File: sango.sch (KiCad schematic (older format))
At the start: 22 parts

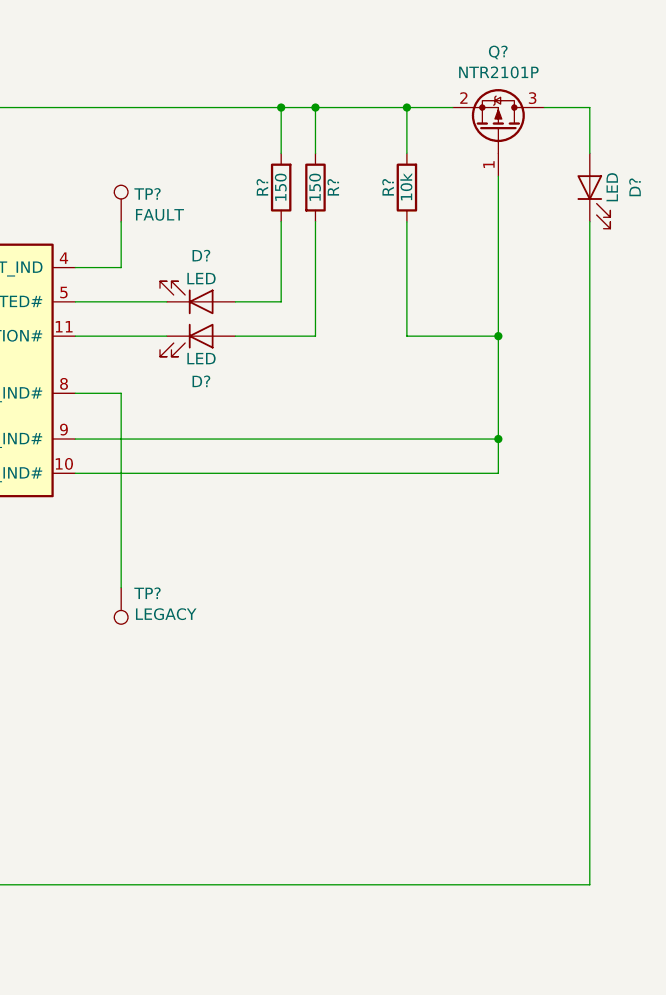
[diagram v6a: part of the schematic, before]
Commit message: add ilim R for output LED
- part numbers for remaining resistors
- rename LEDs for associated color
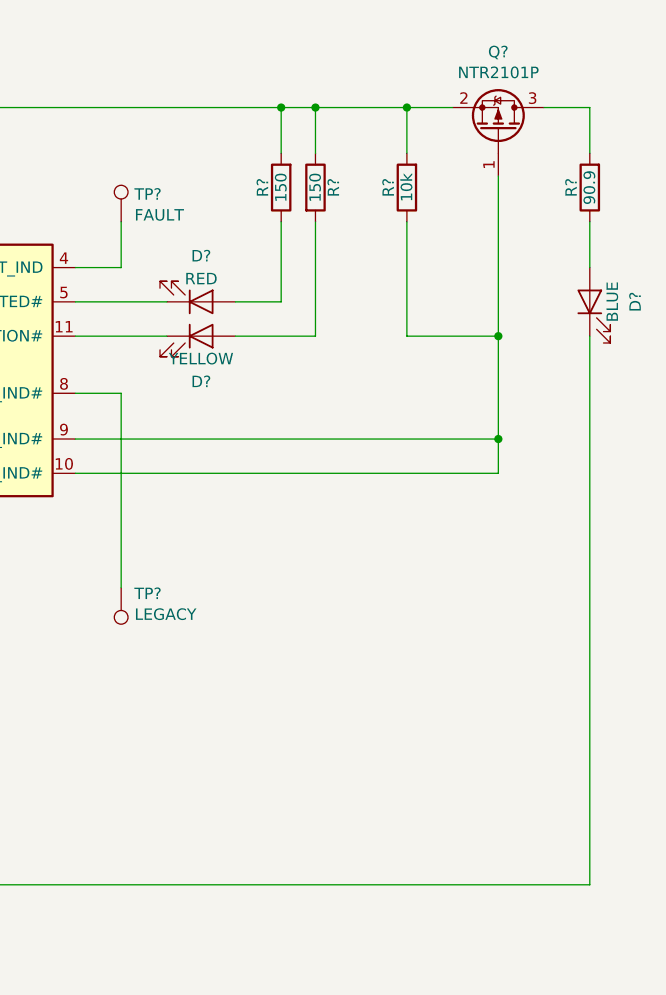
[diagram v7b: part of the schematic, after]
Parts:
- added R?: 90.9, symbol Device:R
- D?: value LED -> YELLOW
- D?: value LED -> RED
- D?: value LED -> BLUE
- R? (x2): Description (none) -> RES SMD 150 OHM 1% 1/10W 0603; Manufacturer (none) -> Panasonic Electronic Components; Manufacturer Part Number (none) -> ERJ-3EKF1500V; Supplier (none) -> Digi-Key; Supplier Part Number (none) -> P150HCT-ND
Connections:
- net at Q?.3 (D): now also R?.2; no longer D?.2 (A)
- new net: D?.2 (A), R?.1
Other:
- moved on the sheet: D?
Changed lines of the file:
@@
 P 7650 3000
 F 0 "D?" H 7650 2800 50  0000 C CNN
-F 1 "LED" H 7650 2900 50  0000 C CNN
+F 1 "YELLOW" H 7650 2900 50  0000 C CNN
 F 2 "" H 7650 3000 50  0001 C CNN
 F 3 "~" H 7650 3000 50  0001 C CNN
@@
 P 7650 2850
 F 0 "D?" H 7650 2650 50  0000 C CNN
-F 1 "LED" H 7650 2750 50  0000 C CNN
+F 1 "RED" H 7650 2750 50  0000 C CNN
 F 2 "" H 7650 2850 50  0001 C CNN
 F 3 "~" H 7650 2850 50  0001 C CNN
@@
 F 1 "150" V 8000 2350 50  0000 C CNN
 F 2 "" V 7930 2350 50  0001 C CNN
-F 3 "" H 8000 2350 50  0001 C CNN
+F 3 "https://industrial.panasonic.com/cdbs/www-data/pdf/RDA0000/AOA0000C304.pdf" H 8000 2350 50  0001 C CNN
+F 4 "RES SMD 150 OHM 1% 1/10W 0603" H 0   0   50  0001 C CNN "Description"
+F 5 "Panasonic Electronic Components" H 0   0   50  0001 C CNN "Manufacturer"
+F 6 "ERJ-3EKF1500V" H 0   0   50  0001 C CNN "Manufacturer Part Number"
+F 7 "Digi-Key" H 0   0   50  0001 C CNN "Supplier"
+F 8 "P150HCT-ND" H 0   0   50  0001 C CNN "Supplier Part Number"
 	1    8000 2350
 	-1   0    0    1
@@
 F 1 "150" V 8150 2350 50  0000 C CNN
 F 2 "" V 8080 2350 50  0001 C CNN
-F 3 "" H 8150 2350 50  0001 C CNN
+F 3 "https://industrial.panasonic.com/cdbs/www-data/pdf/RDA0000/AOA0000C304.pdf" H 8150 2350 50  0001 C CNN
+F 4 "RES SMD 150 OHM 1% 1/10W 0603" H 0   0   50  0001 C CNN "Description"
+F 5 "Panasonic Electronic Components" H 0   0   50  0001 C CNN "Manufacturer"
+F 6 "ERJ-3EKF1500V" H 0   0   50  0001 C CNN "Manufacturer Part Number"
+F 7 "Digi-Key" H 0   0   50  0001 C CNN "Supplier"
+F 8 "P150HCT-ND" H 0   0   50  0001 C CNN "Supplier Part Number"
 	1    8150 2350
 	1    0    0    -1
@@
 L Device:LED D?
 U 1 1 5BF7A803
-P 9350 2350
-F 0 "D?" H 9350 2150 50  0000 C CNN
-F 1 "LED" H 9350 2250 50  0000 C CNN
-F 2 "" H 9350 2350 50  0001 C CNN
-F 3 "~" H 9350 2350 50  0001 C CNN
-	1    9350 2350
+P 9350 2850
+F 0 "D?" H 9350 2650 50  0000 C CNN
+F 1 "BLUE" H 9350 2750 50  0000 C CNN
+F 2 "" H 9350 2850 50  0001 C CNN
+F 3 "~" H 9350 2850 50  0001 C CNN
+	1    9350 2850
 	0    -1   -1   0
 $EndComp
@@
 Wire Wire Line
 	9350 2000 9350 2200
-Wire Wire Line
-	9350 2500 9350 5400
 Wire Wire Line
 	9350 5400 6300 5400
@@
 Wire Wire Line
 	6200 5400 6300 5400
+$Comp
+L Device:R R?
+U 1 1 5BF89938
+P 9350 2350
+F 0 "R?" V 9430 2350 50  0000 C CNN
+F 1 "90.9" V 9350 2350 50  0000 C CNN
+F 2 "" V 9280 2350 50  0001 C CNN
+F 3 "https://industrial.panasonic.com/cdbs/www-data/pdf/RDA0000/AOA0000C304.pdf" H 9350 2350 50  0001 C CNN
+F 4 "RES SMD 90.9 OHM 1% 1/10W 0603" H 0   0   50  0001 C CNN "Description"
+F 5 "Panasonic Electronic Components" H 0   0   50  0001 C CNN "Manufacturer"
+F 6 "ERJ-3EKF90R9V" H 0   0   50  0001 C CNN "Manufacturer Part Number"
+F 7 "Digi-Key" H 0   0   50  0001 C CNN "Supplier"
+F 8 "P90.9HCT-ND" H 0   0   50  0001 C CNN "Supplier Part Number"
+	1    9350 2350
+	-1   0    0    1
+$EndComp
+Wire Wire Line
+	9350 2500 9350 2700
+Wire Wire Line
+	9350 3000 9350 5400
 $EndSCHEMATC

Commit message: switch resistors from 0603 --> 0805
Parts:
- R? (x5): Description RES SMD 10K OHM 1% 1/10W 0603 -> RES SMD 10K OHM 1% 1/8W 0805; Manufacturer Part Number ERJ-3EKF1002V -> ERJ-6ENF1002V; Supplier Part Number P10.0KHCT-ND -> P10.0KCCT-ND
- R? (x3): Description RES SMD 5.1K OHM 1% 1/10W 0603 -> RES SMD 5.1K OHM 1% 1/8W 0805; Manufacturer Part Number ERJ-3EKF5101V -> ERJ-6ENF5101V; Supplier Part Number P5.10KHCT-ND -> P5.10KCCT-ND
- R?: Description RES SMD 35.7K OHM 1% 1/10W 0603 -> RES SMD 35.7K OHM 1% 1/8W 0805; Manufacturer Part Number ERJ-3EKF3572V -> ERJ-6ENF3572V; Supplier Part Number P35.7KHCT-ND -> P35.7KCCT-ND
- R?: Description RES SMD 1M OHM 1% 1/10W 0603 -> RES SMD 1M OHM 1% 1/8W 0805; Manufacturer Part Number ERJ-3EKF1004V -> ERJ-6ENF1004V; Supplier Part Number P1.00MHCT-ND -> P1.00MCCT-ND
- R? (x2): Description RES SMD 150 OHM 1% 1/10W 0603 -> RES SMD 150 OHM 1% 1/8W 0805; Manufacturer Part Number ERJ-3EKF1500V -> ERJ-6ENF1500V; Supplier Part Number P150HCT-ND -> P150CCT-ND
- R?: Description RES SMD 90.9 OHM 1% 1/10W 0603 -> RES SMD 90.9 OHM 1% 1/8W 0805; Manufacturer Part Number ERJ-3EKF90R9V -> ERJ-6ENF90R9V; Supplier Part Number P90.9HCT-ND -> P90.9CCT-ND
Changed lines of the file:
@@
 F 2 "" V 4680 3450 50  0001 C CNN
 F 3 "https://industrial.panasonic.com/cdbs/www-data/pdf/RDA0000/AOA0000C304.pdf" H 4750 3450 50  0001 C CNN
-F 4 "RES SMD 10K OHM 1% 1/10W 0603" H 4750 3450 50  0001 C CNN "Description"
+F 4 "RES SMD 10K OHM 1% 1/8W 0805" H 4750 3450 50  0001 C CNN "Description"
 F 5 "Panasonic Electronic Components" H 4750 3450 50  0001 C CNN "Manufacturer"
-F 6 "ERJ-3EKF1002V" H 4750 3450 50  0001 C CNN "Manufacturer Part Number"
+F 6 "ERJ-6ENF1002V" H 4750 3450 50  0001 C CNN "Manufacturer Part Number"
 F 7 "Digi-Key" H 4750 3450 50  0001 C CNN "Supplier"
-F 8 "P10.0KHCT-ND" H 4750 3450 50  0001 C CNN "Supplier Part Number"
+F 8 "P10.0KCCT-ND" H 4750 3450 50  0001 C CNN "Supplier Part Number"
 	1    4750 3450
 	0    -1   -1   0
@@
 F 2 "" V 4680 3600 50  0001 C CNN
 F 3 "https://industrial.panasonic.com/cdbs/www-data/pdf/RDA0000/AOA0000C304.pdf" H 4750 3600 50  0001 C CNN
-F 4 "RES SMD 10K OHM 1% 1/10W 0603" H 4750 3600 50  0001 C CNN "Description"
+F 4 "RES SMD 10K OHM 1% 1/8W 0805" H 4750 3600 50  0001 C CNN "Description"
 F 5 "Panasonic Electronic Components" H 4750 3600 50  0001 C CNN "Manufacturer"
-F 6 "ERJ-3EKF1002V" H 4750 3600 50  0001 C CNN "Manufacturer Part Number"
+F 6 "ERJ-6ENF1002V" H 4750 3600 50  0001 C CNN "Manufacturer Part Number"
 F 7 "Digi-Key" H 4750 3600 50  0001 C CNN "Supplier"
-F 8 "P10.0KHCT-ND" H 4750 3600 50  0001 C CNN "Supplier Part Number"
+F 8 "P10.0KCCT-ND" H 4750 3600 50  0001 C CNN "Supplier Part Number"
 	1    4750 3600
 	0    1    1    0
@@
 F 2 "" V 4330 3950 50  0001 C CNN
 F 3 "https://industrial.panasonic.com/cdbs/www-data/pdf/RDA0000/AOA0000C304.pdf" H 4400 3950 50  0001 C CNN
-F 4 "RES SMD 5.1K OHM 1% 1/10W 0603" H 4400 3950 50  0001 C CNN "Description"
+F 4 "RES SMD 5.1K OHM 1% 1/8W 0805" H 4400 3950 50  0001 C CNN "Description"
 F 5 "Panasonic Electronic Components" H 4400 3950 50  0001 C CNN "Manufacturer"
-F 6 "ERJ-3EKF5101V" H 4400 3950 50  0001 C CNN "Manufacturer Part Number"
+F 6 "ERJ-6ENF5101V" H 4400 3950 50  0001 C CNN "Manufacturer Part Number"
 F 7 "Digi-Key" H 4400 3950 50  0001 C CNN "Supplier"
-F 8 "P5.10KHCT-ND" H 4400 3950 50  0001 C CNN "Supplier Part Number"
+F 8 "P5.10KCCT-ND" H 4400 3950 50  0001 C CNN "Supplier Part Number"
 	1    4400 3950
 	1    0    0    -1
@@
 F 2 "" V 4180 3950 50  0001 C CNN
 F 3 "https://industrial.panasonic.com/cdbs/www-data/pdf/RDA0000/AOA0000C304.pdf" H 4250 3950 50  0001 C CNN
-F 4 "RES SMD 5.1K OHM 1% 1/10W 0603" H 4250 3950 50  0001 C CNN "Description"
+F 4 "RES SMD 5.1K OHM 1% 1/8W 0805" H 4250 3950 50  0001 C CNN "Description"
 F 5 "Panasonic Electronic Components" H 4250 3950 50  0001 C CNN "Manufacturer"
-F 6 "ERJ-3EKF5101V" H 4250 3950 50  0001 C CNN "Manufacturer Part Number"
+F 6 "ERJ-6ENF5101V" H 4250 3950 50  0001 C CNN "Manufacturer Part Number"
 F 7 "Digi-Key" H 4250 3950 50  0001 C CNN "Supplier"
-F 8 "P5.10KHCT-ND" H 4250 3950 50  0001 C CNN "Supplier Part Number"
+F 8 "P5.10KCCT-ND" H 4250 3950 50  0001 C CNN "Supplier Part Number"
 	1    4250 3950
 	-1   0    0    1
@@
 F 2 "" V 4930 2350 50  0001 C CNN
 F 3 "https://industrial.panasonic.com/cdbs/www-data/pdf/RDA0000/AOA0000C304.pdf" H 5000 2350 50  0001 C CNN
-F 4 "RES SMD 10K OHM 1% 1/10W 0603" H 5000 2350 50  0001 C CNN "Description"
+F 4 "RES SMD 10K OHM 1% 1/8W 0805" H 5000 2350 50  0001 C CNN "Description"
 F 5 "Panasonic Electronic Components" H 5000 2350 50  0001 C CNN "Manufacturer"
-F 6 "ERJ-3EKF1002V" H 5000 2350 50  0001 C CNN "Manufacturer Part Number"
+F 6 "ERJ-6ENF1002V" H 5000 2350 50  0001 C CNN "Manufacturer Part Number"
 F 7 "Digi-Key" H 5000 2350 50  0001 C CNN "Supplier"
-F 8 "P10.0KHCT-ND" H 5000 2350 50  0001 C CNN "Supplier Part Number"
+F 8 "P10.0KCCT-ND" H 5000 2350 50  0001 C CNN "Supplier Part Number"
 	1    5000 2350
 	-1   0    0    1
@@
 F 2 "" V 5080 2350 50  0001 C CNN
 F 3 "https://industrial.panasonic.com/cdbs/www-data/pdf/RDA0000/AOA0000C304.pdf" H 5150 2350 50  0001 C CNN
-F 4 "RES SMD 10K OHM 1% 1/10W 0603" H 5150 2350 50  0001 C CNN "Description"
+F 4 "RES SMD 10K OHM 1% 1/8W 0805" H 5150 2350 50  0001 C CNN "Description"
 F 5 "Panasonic Electronic Components" H 5150 2350 50  0001 C CNN "Manufacturer"
-F 6 "ERJ-3EKF1002V" H 5150 2350 50  0001 C CNN "Manufacturer Part Number"
+F 6 "ERJ-6ENF1002V" H 5150 2350 50  0001 C CNN "Manufacturer Part Number"
 F 7 "Digi-Key" H 5150 2350 50  0001 C CNN "Supplier"
-F 8 "P10.0KHCT-ND" H 5150 2350 50  0001 C CNN "Supplier Part Number"
+F 8 "P10.0KCCT-ND" H 5150 2350 50  0001 C CNN "Supplier Part Number"
 	1    5150 2350
 	1    0    0    -1
@@
 F 2 "" V 3880 3250 50  0001 C CNN
 F 3 "https://industrial.panasonic.com/cdbs/www-data/pdf/RDA0000/AOA0000C304.pdf" H 3950 3250 50  0001 C CNN
-F 4 "RES SMD 5.1K OHM 1% 1/10W 0603" H 3950 3250 50  0001 C CNN "Description"
+F 4 "RES SMD 5.1K OHM 1% 1/8W 0805" H 3950 3250 50  0001 C CNN "Description"
 F 5 "Panasonic Electronic Components" H 3950 3250 50  0001 C CNN "Manufacturer"
-F 6 "ERJ-3EKF5101V" H 3950 3250 50  0001 C CNN "Manufacturer Part Number"
+F 6 "ERJ-6ENF5101V" H 3950 3250 50  0001 C CNN "Manufacturer Part Number"
 F 7 "Digi-Key" H 3950 3250 50  0001 C CNN "Supplier"
-F 8 "P5.10KHCT-ND" H 3950 3250 50  0001 C CNN "Supplier Part Number"
+F 8 "P5.10KCCT-ND" H 3950 3250 50  0001 C CNN "Supplier Part Number"
 	1    3950 3250
 	-1   0    0    1
@@
 F 2 "" V 3880 2850 50  0001 C CNN
 F 3 "https://industrial.panasonic.com/cdbs/www-data/pdf/RDA0000/AOA0000C304.pdf" H 3950 2850 50  0001 C CNN
-F 4 "RES SMD 35.7K OHM 1% 1/10W 0603" H 3950 2850 50  0001 C CNN "Description"
+F 4 "RES SMD 35.7K OHM 1% 1/8W 0805" H 3950 2850 50  0001 C CNN "Description"
 F 5 "Panasonic Electronic Components" H 3950 2850 50  0001 C CNN "Manufacturer"
-F 6 "ERJ-3EKF3572V" H 3950 2850 50  0001 C CNN "Manufacturer Part Number"
+F 6 "ERJ-6ENF3572V" H 3950 2850 50  0001 C CNN "Manufacturer Part Number"
 F 7 "Digi-Key" H 3950 2850 50  0001 C CNN "Supplier"
-F 8 "P35.7KHCT-ND" H 3950 2850 50  0001 C CNN "Supplier Part Number"
+F 8 "P35.7KCCT-ND" H 3950 2850 50  0001 C CNN "Supplier Part Number"
 	1    3950 2850
 	-1   0    0    1
@@
 F 2 "" V 2580 5150 50  0001 C CNN
 F 3 "https://industrial.panasonic.com/cdbs/www-data/pdf/RDA0000/AOA0000C304.pdf" H 2650 5150 50  0001 C CNN
-F 4 "RES SMD 1M OHM 1% 1/10W 0603" H 2650 5150 50  0001 C CNN "Description"
+F 4 "RES SMD 1M OHM 1% 1/8W 0805" H 2650 5150 50  0001 C CNN "Description"
 F 5 "Panasonic Electronic Components" H 2650 5150 50  0001 C CNN "Manufacturer"
-F 6 "ERJ-3EKF1004V" H 2650 5150 50  0001 C CNN "Manufacturer Part Number"
+F 6 "ERJ-6ENF1004V" H 2650 5150 50  0001 C CNN "Manufacturer Part Number"
 F 7 "Digi-Key" H 2650 5150 50  0001 C CNN "Supplier"
-F 8 "P1.00MHCT-ND" H 2650 5150 50  0001 C CNN "Supplier Part Number"
+F 8 "P1.00MCCT-ND" H 2650 5150 50  0001 C CNN "Supplier Part Number"
 	1    2650 5150
 	1    0    0    1
@@
 F 2 "" V 8480 2350 50  0001 C CNN
 F 3 "https://industrial.panasonic.com/cdbs/www-data/pdf/RDA0000/AOA0000C304.pdf" H 8550 2350 50  0001 C CNN
-F 4 "RES SMD 10K OHM 1% 1/10W 0603" H 8550 2350 50  0001 C CNN "Description"
+F 4 "RES SMD 10K OHM 1% 1/8W 0805" H 8550 2350 50  0001 C CNN "Description"
 F 5 "Panasonic Electronic Components" H 8550 2350 50  0001 C CNN "Manufacturer"
-F 6 "ERJ-3EKF1002V" H 8550 2350 50  0001 C CNN "Manufacturer Part Number"
+F 6 "ERJ-6ENF1002V" H 8550 2350 50  0001 C CNN "Manufacturer Part Number"
 F 7 "Digi-Key" H 8550 2350 50  0001 C CNN "Supplier"
-F 8 "P10.0KHCT-ND" H 8550 2350 50  0001 C CNN "Supplier Part Number"
+F 8 "P10.0KCCT-ND" H 8550 2350 50  0001 C CNN "Supplier Part Number"
 	1    8550 2350
 	-1   0    0    1
@@
 F 2 "" V 7930 2350 50  0001 C CNN
 F 3 "https://industrial.panasonic.com/cdbs/www-data/pdf/RDA0000/AOA0000C304.pdf" H 8000 2350 50  0001 C CNN
-F 4 "RES SMD 150 OHM 1% 1/10W 0603" H 0   0   50  0001 C CNN "Description"
+F 4 "RES SMD 150 OHM 1% 1/8W 0805" H 0   0   50  0001 C CNN "Description"
 F 5 "Panasonic Electronic Components" H 0   0   50  0001 C CNN "Manufacturer"
-F 6 "ERJ-3EKF1500V" H 0   0   50  0001 C CNN "Manufacturer Part Number"
+F 6 "ERJ-6ENF1500V" H 0   0   50  0001 C CNN "Manufacturer Part Number"
 F 7 "Digi-Key" H 0   0   50  0001 C CNN "Supplier"
-F 8 "P150HCT-ND" H 0   0   50  0001 C CNN "Supplier Part Number"
+F 8 "P150CCT-ND" H 0   0   50  0001 C CNN "Supplier Part Number"
 	1    8000 2350
 	-1   0    0    1
@@
 F 2 "" V 8080 2350 50  0001 C CNN
 F 3 "https://industrial.panasonic.com/cdbs/www-data/pdf/RDA0000/AOA0000C304.pdf" H 8150 2350 50  0001 C CNN
-F 4 "RES SMD 150 OHM 1% 1/10W 0603" H 0   0   50  0001 C CNN "Description"
+F 4 "RES SMD 150 OHM 1% 1/8W 0805" H 0   0   50  0001 C CNN "Description"
 F 5 "Panasonic Electronic Components" H 0   0   50  0001 C CNN "Manufacturer"
-F 6 "ERJ-3EKF1500V" H 0   0   50  0001 C CNN "Manufacturer Part Number"
+F 6 "ERJ-6ENF1500V" H 0   0   50  0001 C CNN "Manufacturer Part Number"
 F 7 "Digi-Key" H 0   0   50  0001 C CNN "Supplier"
-F 8 "P150HCT-ND" H 0   0   50  0001 C CNN "Supplier Part Number"
+F 8 "P150CCT-ND" H 0   0   50  0001 C CNN "Supplier Part Number"
 	1    8150 2350
 	1    0    0    -1
@@
 F 2 "" V 9280 2350 50  0001 C CNN
 F 3 "https://industrial.panasonic.com/cdbs/www-data/pdf/RDA0000/AOA0000C304.pdf" H 9350 2350 50  0001 C CNN
-F 4 "RES SMD 90.9 OHM 1% 1/10W 0603" H 0   0   50  0001 C CNN "Description"
+F 4 "RES SMD 90.9 OHM 1% 1/8W 0805" H 0   0   50  0001 C CNN "Description"
 F 5 "Panasonic Electronic Components" H 0   0   50  0001 C CNN "Manufacturer"
-F 6 "ERJ-3EKF90R9V" H 0   0   50  0001 C CNN "Manufacturer Part Number"
+F 6 "ERJ-6ENF90R9V" H 0   0   50  0001 C CNN "Manufacturer Part Number"
 F 7 "Digi-Key" H 0   0   50  0001 C CNN "Supplier"
-F 8 "P90.9HCT-ND" H 0   0   50  0001 C CNN "Supplier Part Number"
+F 8 "P90.9CCT-ND" H 0   0   50  0001 C CNN "Supplier Part Number"
 	1    9350 2350
 	-1   0    0    1
